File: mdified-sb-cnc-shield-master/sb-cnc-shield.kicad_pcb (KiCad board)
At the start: 2 copper layers, 68.6 x 53.3 mm, 62 parts, among them P1 XMOT, P2 YMOT, P3 ZMOT, P4 AMOT, P5 UART, P6 I2C, P7 ES_SETUP, P8 12V-36V, SW1 RESET, U1 ARDUINO_UNO_SHIELD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

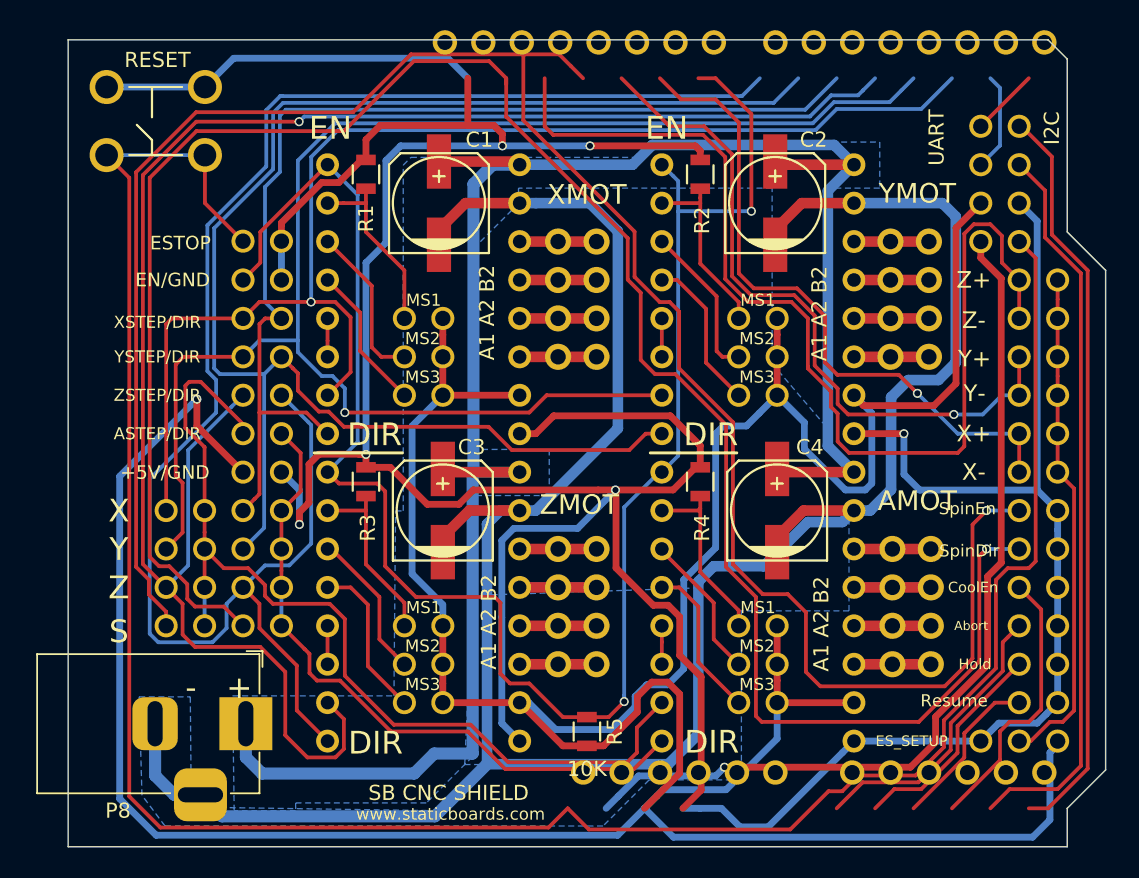
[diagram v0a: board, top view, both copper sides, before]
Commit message: add jack barrel for power supply in kicad, correction
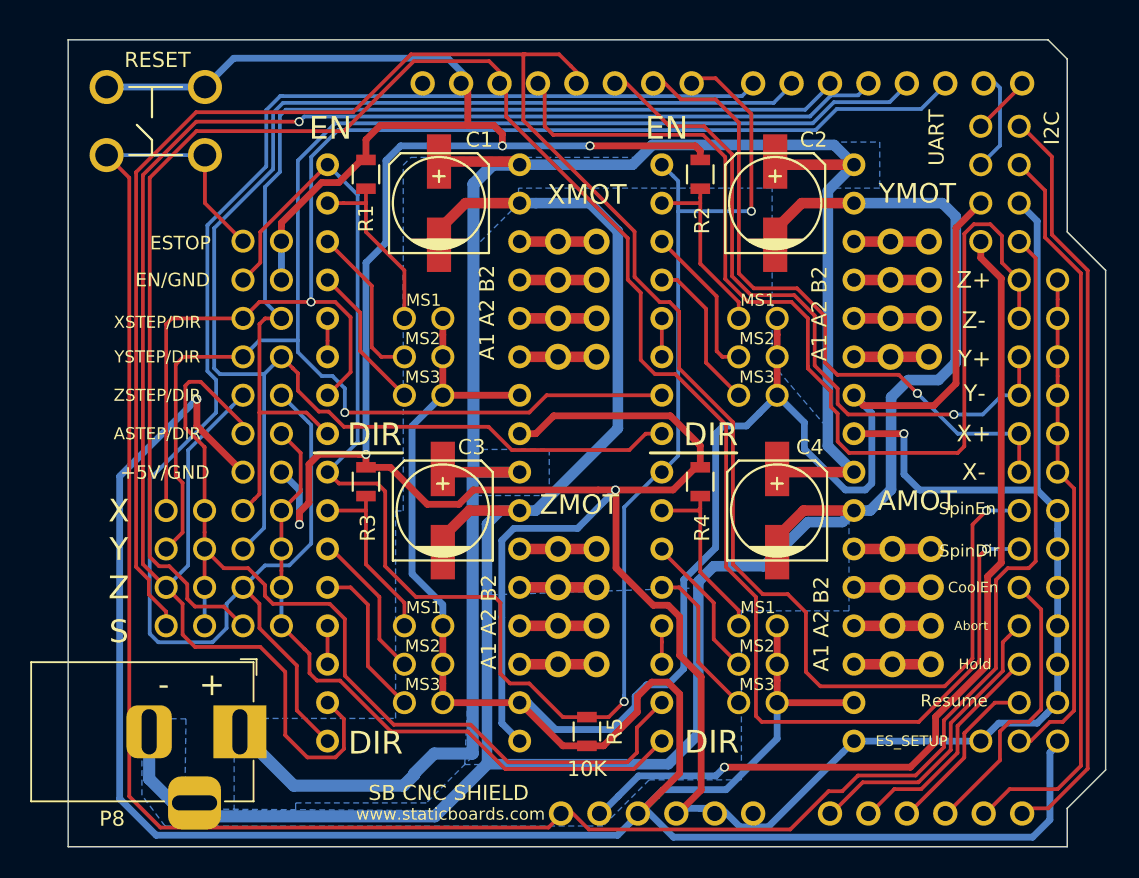
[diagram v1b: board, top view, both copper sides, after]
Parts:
- moved U1 3.08 mm to (113.9, 119.7)
- moved P8 0.66 mm to (125.7, 111.8)
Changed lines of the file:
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@@
   (general
     (thickness 1.6)
-    (drawings 44)
-    (tracks 777)
+    (drawings 42)
+    (tracks 778)
     (zones 0)
     (modules 62)
@@
     (mod_text_size 1 1)
     (mod_text_width 0.15)
-    (pad_size 3.5 3.5)
-    (pad_drill 3)
+    (pad_size 1.51 1.51)
+    (pad_drill 0.9)
     (pad_to_mask_clearance 0)
     (aux_axis_origin 0 0)
@@
   )
   (module footprints:ARDUINO_SHIELD (layer F.Cu)
-    (at 115.32616 117.01272)
+    (at 113.85804 119.72036)
     (fp_text reference U1 (at 5.715 -57.15) (layer F.SilkS) hide
       (effects (font (size 1.524 1.524) (thickness 0.3048)))
@@
   )
   (module Connector_BarrelJack:BarrelJack_Horizontal (layer F.Cu)
-    (at 126.04496 111.24692)
+    (at 125.6538 111.78032)
     (descr "DC Barrel Jack")
     (tags "Power Jack")
@@
     )
   )
-  (dimension 6.076224 (width 0.15) (layer Dwgs.User)
-    (gr_text "6,076 mm" (at 123.031954 125.994536 -0.766453001) (layer Dwgs.User)
-      (effects (font (size 1 1) (thickness 0.15)))
-    )
-    (feature1 (pts (xy 120.18264 111.8616) (xy 120.00366 125.240381)))
-    (feature2 (pts (xy 126.25832 111.94288) (xy 126.07934 125.321661)))
-    (crossbar (pts (xy 126.087184 124.735292) (xy 120.011504 124.654012)))
-    (arrow1a (pts (xy 120.011504 124.654012) (xy 121.145751 124.082713)))
-    (arrow1b (pts (xy 120.011504 124.654012) (xy 121.130063 125.255449)))
-    (arrow2a (pts (xy 126.087184 124.735292) (xy 124.968625 124.133855)))
-    (arrow2b (pts (xy 126.087184 124.735292) (xy 124.952937 125.306591)))
-  )
-  (dimension 6.177355 (width 0.15) (layer Dwgs.User)
-    (gr_text "6,177 mm" (at 106.643153 113.390139 89.71729286) (layer Dwgs.User)
-      (effects (font (size 1 1) (thickness 0.15)))
-    )
-    (feature1 (pts (xy 123.2408 110.38332) (xy 107.371963 110.30502)))
-    (feature2 (pts (xy 123.21032 116.5606) (xy 107.341483 116.4823)))
-    (crossbar (pts (xy 107.927897 116.485193) (xy 107.958377 110.307913)))
-    (arrow1a (pts (xy 107.958377 110.307913) (xy 108.539232 111.437297)))
-    (arrow1b (pts (xy 107.958377 110.307913) (xy 107.366405 111.43151)))
-    (arrow2a (pts (xy 107.927897 116.485193) (xy 108.519869 115.361596)))
-    (arrow2b (pts (xy 107.927897 116.485193) (xy 107.347042 115.355809)))
-  )
   (gr_text MS3 (at 159.8295 88.3285) (layer F.SilkS)
     (effects (font (size 0.8 0.8) (thickness 0.125)))
@@
     (effects (font (size 1.5 1.5) (thickness 0.3)))
   )
-  (gr_text "-   +" (at 124.2568 108.8644) (layer F.SilkS)
+  (gr_text "-   +" (at 122.4534 108.6612) (layer F.SilkS)
     (effects (font (size 1.5 1.5) (thickness 0.3)))
   )
@@
   (segment (start 126.944001 96.067999) (end 126.618999 96.393001) (width 0.25) (layer F.Cu) (net 38))
   (segment (start 126.618999 96.393001) (end 125.857 97.155) (width 0.25) (layer F.Cu) (net 38))
+  (segment (start 137.175999 114.538001) (end 138.49599 113.21801) (width 0.8) (layer B.Cu) (net 39))
+  (segment (start 138.49599 113.21801) (end 141.03599 113.21801) (width 0.8) (layer B.Cu) (net 39))
+  (segment (start 141.03599 113.21801) (end 141.03599 94.66923) (width 0.8) (layer B.Cu) (net 39))
+  (segment (start 141.03599 94.66923) (end 141.09022 94.615) (width 0.8) (layer B.Cu) (net 39))
   (segment (start 141.09022 94.615) (end 141.09022 75.57178) (width 0.8) (layer B.Cu) (net 39))
   (segment (start 141.09022 75.57178) (end 142.367 74.295) (width 0.8) (layer B.Cu) (net 39))
@@
   (segment (start 138.811 74.08418) (end 143.93418 74.08418) (width 0.7) (layer F.Cu) (net 39))
   (segment (start 143.93418 74.08418) (end 144.145 74.295) (width 0.7) (layer F.Cu) (net 39))
-  (segment (start 126.04496 113.46688) (end 126.04496 111.24692) (width 0.8) (layer B.Cu) (net 39))
-  (segment (start 137.175999 114.538001) (end 127.116081 114.538001) (width 0.8) (layer B.Cu) (net 39))
-  (segment (start 138.49599 113.21801) (end 137.175999 114.538001) (width 0.8) (layer B.Cu) (net 39))
-  (segment (start 141.03599 113.21801) (end 138.49599 113.21801) (width 0.8) (layer B.Cu) (net 39))
-  (segment (start 127.116081 114.538001) (end 126.04496 113.46688) (width 0.8) (layer B.Cu) (net 39))
-  (segment (start 141.03599 94.66923) (end 141.03599 113.21801) (width 0.8) (layer B.Cu) (net 39))
-  (segment (start 141.09022 94.615) (end 141.03599 94.66923) (width 0.8) (layer B.Cu) (net 39))
+  (segment (start 137.175999 114.538001) (end 137.175999 114.629441) (width 0.8) (layer B.Cu) (net 39))
+  (segment (start 137.175999 114.629441) (end 136.46404 115.3414) (width 0.8) (layer B.Cu) (net 39))
+  (segment (start 129.21488 115.3414) (end 125.6538 111.78032) (width 0.8) (layer B.Cu) (net 39))
+  (segment (start 136.46404 115.3414) (end 129.21488 115.3414) (width 0.8) (layer B.Cu) (net 39))
   (segment (start 163.519421 71.558989) (end 164.918399 70.160011) (width 0.25) (layer B.Cu) (net 40))
   (segment (start 164.918399 70.160011) (end 168.599989 70.160011) (width 0.25) (layer B.Cu) (net 40))
@@
   (segment (start 162.91433 97.155) (end 161.163 98.90633) (width 0.7) (layer F.Cu) (net 61))
   (segment (start 161.163 98.90633) (end 161.163 99.90582) (width 0.7) (layer F.Cu) (net 61))
-  (segment (start 124.46795 117.36991) (end 123.04496 115.94692) (width 0.8) (layer B.Cu) (net 61))
-  (segment (start 138.537896 117.36991) (end 124.46795 117.36991) (width 0.8) (layer B.Cu) (net 61))
-  (segment (start 123.04496 115.94692) (end 121.31648 115.94692) (width 0.8) (layer B.Cu) (net 61))
-  (segment (start 120.04496 114.6754) (end 120.04496 111.24692) (width 0.8) (layer B.Cu) (net 61))
-  (segment (start 121.31648 115.94692) (end 120.04496 114.6754) (width 0.8) (layer B.Cu) (net 61))
+  (segment (start 123.54339 117.36991) (end 122.6538 116.48032) (width 0.8) (layer B.Cu) (net 61))
+  (segment (start 138.537896 117.36991) (end 123.54339 117.36991) (width 0.8) (layer B.Cu) (net 61))
+  (segment (start 122.6538 116.48032) (end 121.24536 116.48032) (width 0.8) (layer B.Cu) (net 61))
+  (segment (start 119.6538 114.88876) (end 119.6538 111.78032) (width 0.8) (layer B.Cu) (net 61))
+  (segment (start 121.24536 116.48032) (end 119.6538 114.88876) (width 0.8) (layer B.Cu) (net 61))
   (zone (net 39) (net_name VIN) (layer B.Cu) (hatch edge 0.508)
     (connect_pads yes (clearance 0.508))
@@
         (xy 160.8328 87.5284) (xy 160.8328 75.8444) (xy 144.0688 75.8444) (xy 144.0688 76.8604) (xy 141.0208 79.9084)
         (xy 141.0208 93.1164) (xy 146.1008 93.1164) (xy 146.1008 96.1644) (xy 141.0208 96.1644) (xy 141.0208 113.4364)
-        (xy 137.9728 116.4844) (xy 129.3368 116.4844) (xy 129.3368 116.9924) (xy 125.2728 116.9924) (xy 125.16612 109.40288)
-        (xy 135.83412 109.40288) (xy 135.9408 97.1804) (xy 136.4488 97.1804) (xy 136.4488 74.3204) (xy 136.9568 73.8124)
-        (xy 151.6888 73.8124) (xy 152.7048 72.7964) (xy 167.9448 72.7964)
+        (xy 137.9728 116.4844) (xy 129.3368 116.4844) (xy 129.3368 116.9924) (xy 125.2728 116.9924) (xy 125.2728 110.8964)
+        (xy 135.9408 110.8964) (xy 135.9408 97.1804) (xy 136.4488 97.1804) (xy 136.4488 74.3204) (xy 136.9568 73.8124)
+        (xy 151.6888 73.8124) (xy 152.7048 72.7964) (xy 167.9448 72.7964) (xy 167.9448 75.8444)
       )
     )
@@
       (pts
         (xy 165.9128 103.7844) (xy 158.8008 103.7844) (xy 158.8008 114.9604) (xy 152.7048 114.9604) (xy 149.6568 118.0084)
-        (xy 120.7008 118.0084) (xy 119.1768 115.9764) (xy 118.99392 109.46892) (xy 122.37212 109.46892) (xy 122.43816 116.75872)
+        (xy 120.7008 118.0084) (xy 119.1768 115.9764) (xy 119.1768 110.8964) (xy 122.08764 110.92688) (xy 122.00636 116.88064)
         (xy 138.4808 116.9924) (xy 141.5288 113.9444) (xy 140.5128 113.9444) (xy 141.0208 102.7684) (xy 155.7528 102.277333)
         (xy 155.7528 101.7524) (xy 156.7688 100.7364) (xy 160.3248 100.7364) (xy 163.3728 97.6884) (xy 165.9128 97.6884)

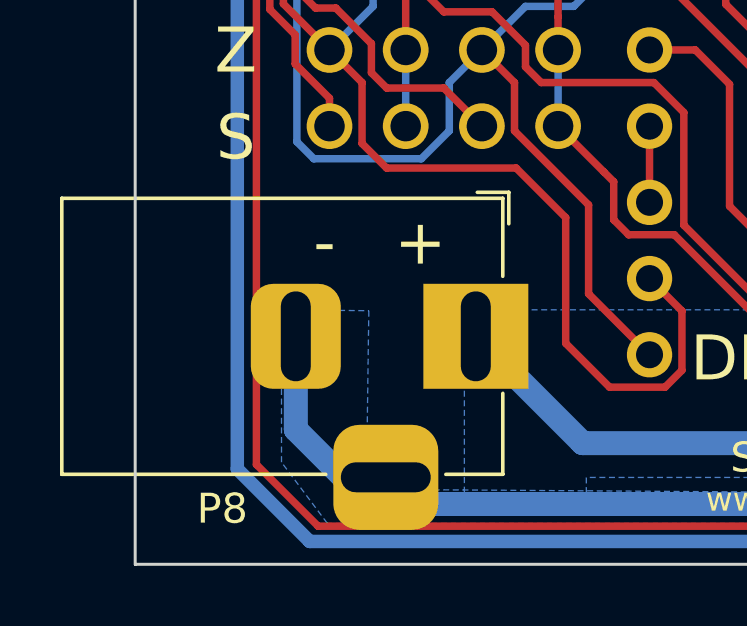
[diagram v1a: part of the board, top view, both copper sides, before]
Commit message: modify jack barrel position for power supply in kicad
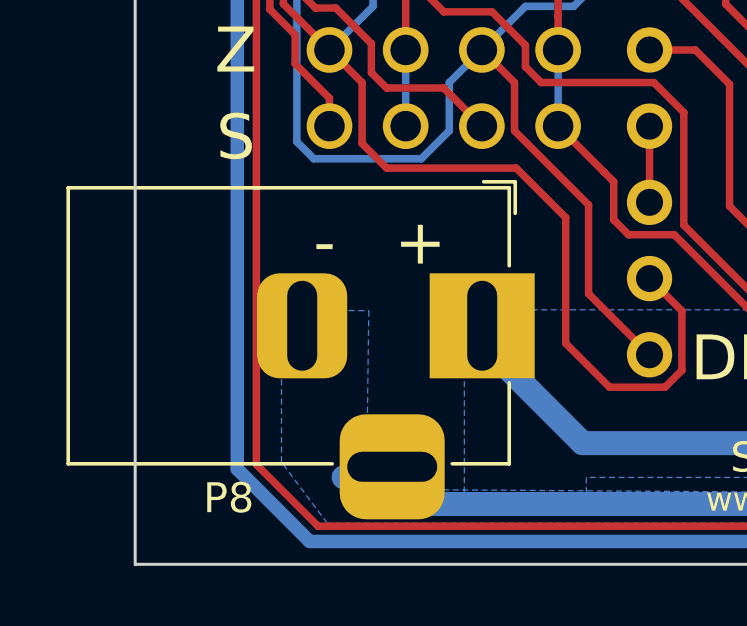
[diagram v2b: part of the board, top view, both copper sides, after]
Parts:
- moved P8 0.41 mm to (125.9, 111.4)
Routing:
- net GNDA: track 171.2 -> 165.8 mm
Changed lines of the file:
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@@
     (thickness 1.6)
     (drawings 42)
-    (tracks 778)
+    (tracks 776)
     (zones 0)
     (modules 62)
@@
   )
   (module Connector_BarrelJack:BarrelJack_Horizontal (layer F.Cu)
-    (at 125.6538 111.78032)
+    (at 125.86768 111.4298)
     (descr "DC Barrel Jack")
     (tags "Power Jack")
@@
   (segment (start 138.537896 117.36991) (end 123.54339 117.36991) (width 0.8) (layer B.Cu) (net 61))
   (segment (start 122.6538 116.48032) (end 121.24536 116.48032) (width 0.8) (layer B.Cu) (net 61))
-  (segment (start 119.6538 114.88876) (end 119.6538 111.78032) (width 0.8) (layer B.Cu) (net 61))
-  (segment (start 121.24536 116.48032) (end 119.6538 114.88876) (width 0.8) (layer B.Cu) (net 61))
   (zone (net 39) (net_name VIN) (layer B.Cu) (hatch edge 0.508)
     (connect_pads yes (clearance 0.508))

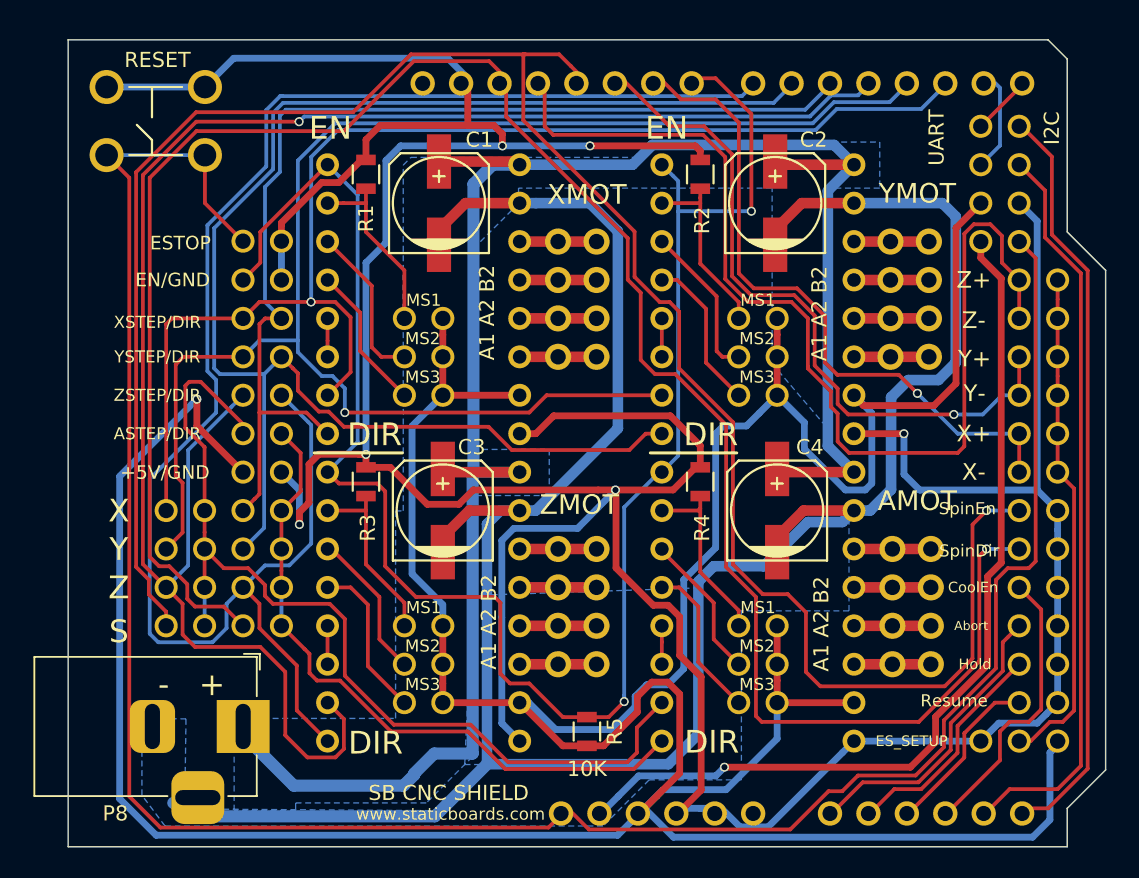
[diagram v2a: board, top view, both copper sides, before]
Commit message: modify the 4 capacitors foorprint and rotate MS1/2/3 connector
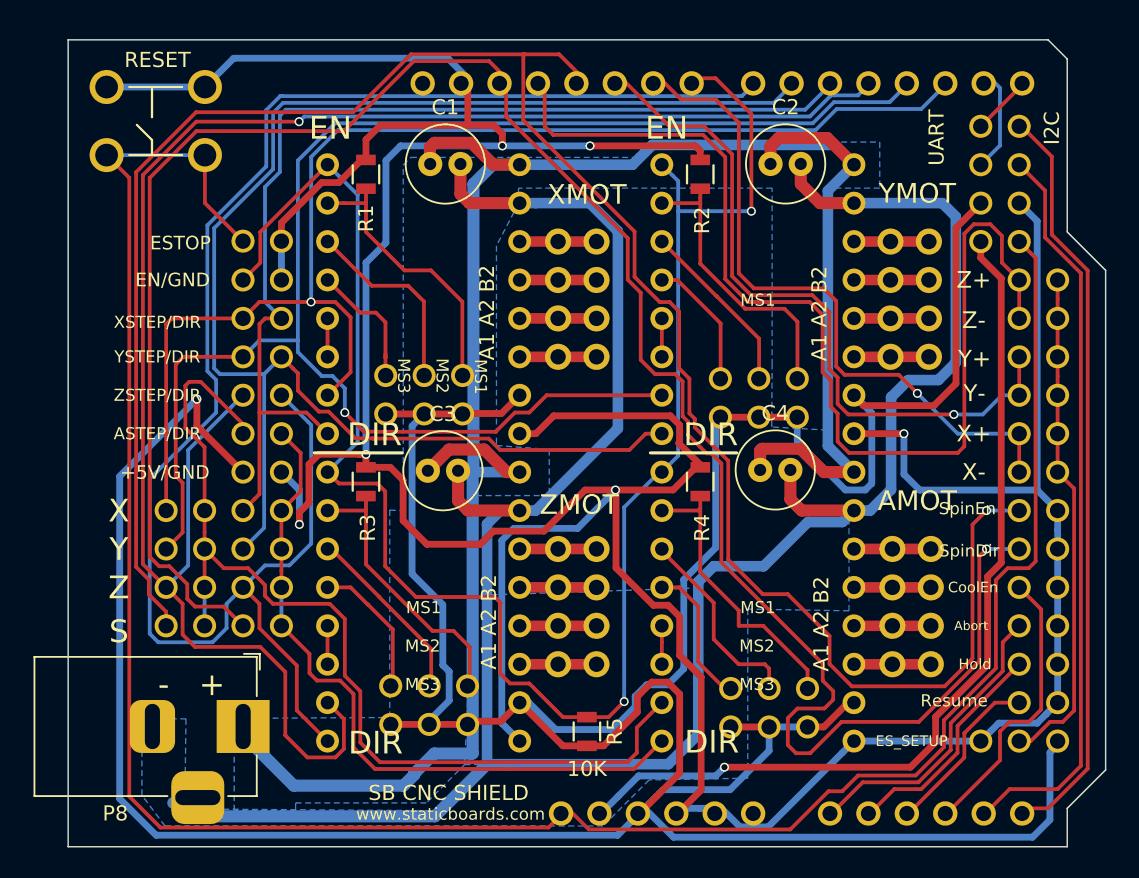
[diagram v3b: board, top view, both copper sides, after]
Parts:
- C1, C2, C3, C4: footprint Capacitors_SMD:c_elec_6.3x7.7 -> Capacitor_THT:C_Radial_D5.0mm_H11.0mm_P2.00mm
- moved JP10 6.98 mm to (163.2, 111.5), turned to 180 degrees
- moved JP7 6.72 mm to (140.7, 111.3), turned to 180 degrees
- moved JP4 6.66 mm to (162.5, 91.0), turned to 180 degrees
- moved JP1 6.45 mm to (140.4, 90.8), turned to 180 degrees
- moved JP11 4.18 mm to (160.6, 111.5), turned to 180 degrees
- moved JP5 4.17 mm to (160.0, 91.0), turned to 180 degrees
- moved JP8 4.08 mm to (138.2, 111.3), turned to 180 degrees
- moved JP6 4.02 mm to (157.4, 91.0), turned to 180 degrees
- moved JP2 3.97 mm to (137.8, 90.8), turned to 180 degrees
- moved JP3 3.97 mm to (135.3, 90.8), turned to 180 degrees
- moved JP9 3.73 mm to (135.6, 111.3), turned to 180 degrees
- moved JP12 3.46 mm to (158.1, 111.5), turned to 180 degrees
- moved C4 2.91 mm to (160.0, 94.5), turned to 0 degrees
- moved C3 2.81 mm to (138.1, 94.5), turned to 0 degrees
- moved C1 2.65 mm to (138.2, 74.2), turned to 0 degrees
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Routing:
- net VIN: track 128.4 -> 139.2 mm
- net Net-(JP4-Pad2): track 12.3 -> 19.4 mm
- net Net-(JP10-Pad2): track 12.3 -> 19.3 mm
- net Net-(JP7-Pad2): track 12.2 -> 18.8 mm
- net Net-(JP1-Pad2): track 12.2 -> 18.6 mm
- net +5V: track 264.8 -> 259.4 mm
- net SPIN_DIR: track 137.4 -> 142.8 mm
- net GND: track 270.3 -> 274.2 mm
- net Net-(JP11-Pad2): track 9.72 -> 13.2 mm
- net GNDA: track 165.8 -> 162.5 mm
- net ADIR: track 44.3 -> 46.9 mm
- net Net-(JP2-Pad2): track 10.6 -> 12.9 mm
- net Net-(JP8-Pad2): track 9.98 -> 12.2 mm
- net ASTEP: track 63.6 -> 65.6 mm
- net Net-(JP6-Pad2): track 10.3 -> 8.74 mm
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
